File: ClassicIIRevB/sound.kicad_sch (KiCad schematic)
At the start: 56 parts, among them J1 SND OUT, J7 SND IN, Q2 MMBTA14, U1 MC34119, U11 LM3080, U2 78L08

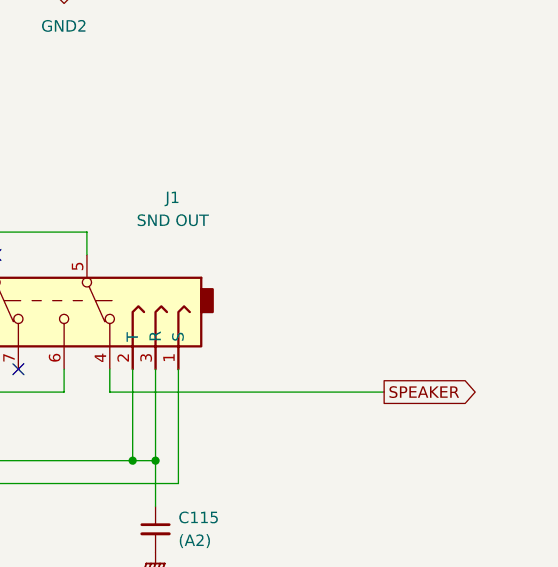
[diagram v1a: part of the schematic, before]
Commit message: improved footprints and silkscreens
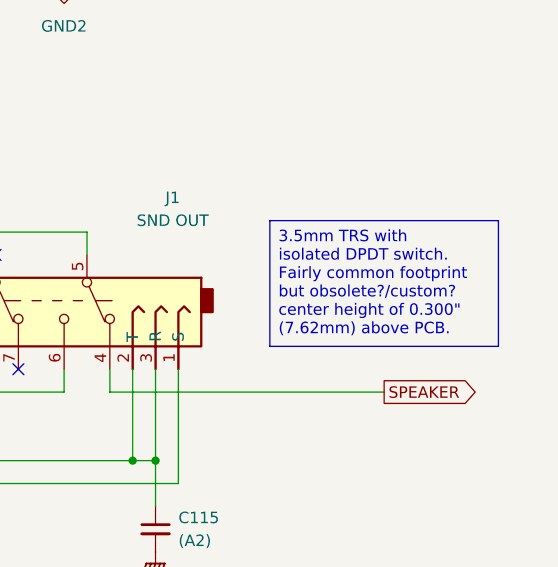
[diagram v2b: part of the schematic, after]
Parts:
- J1: footprint Connector_Mine:SJ3579AN -> Connector_Mine:Jack_3.5mm_SameSky_SJ3589ANG
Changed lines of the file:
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@@
 	(title_block
 		(title "Macintosh Classic II Revision B")
-		(date "2025-05-31")
+		(date "2025-06-04")
 		(company "Apple Computer")
 		(comment 1 "drawn by Bradley Bell")
@@
 		)
 	)
+	(text_box "3.5mm TRS with isolated DPDT switch.\nFairly common footprint but obsolete?/custom? center height of 0.300\" (7.62mm) above PCB."
+		(exclude_from_sim no)
+		(at 228.6 110.49 0)
+		(size 25.4 13.97)
+		(margins 0.9525 0.9525 0.9525 0.9525)
+		(stroke
+			(width 0)
+			(type solid)
+		)
+		(fill
+			(type none)
+		)
+		(effects
+			(font
+				(size 1.27 1.27)
+			)
+			(justify left top)
+		)
+	)
 	(junction
 		(at 165.1 137.16)
@@
 			)
 		)
-		(property "Footprint" "Connector_Mine:SJ3579AN"
+		(property "Footprint" "Connector_Mine:Jack_3.5mm_SameSky_SJ3589ANG"
 			(at 215.9 119.38 0)
 			(effects

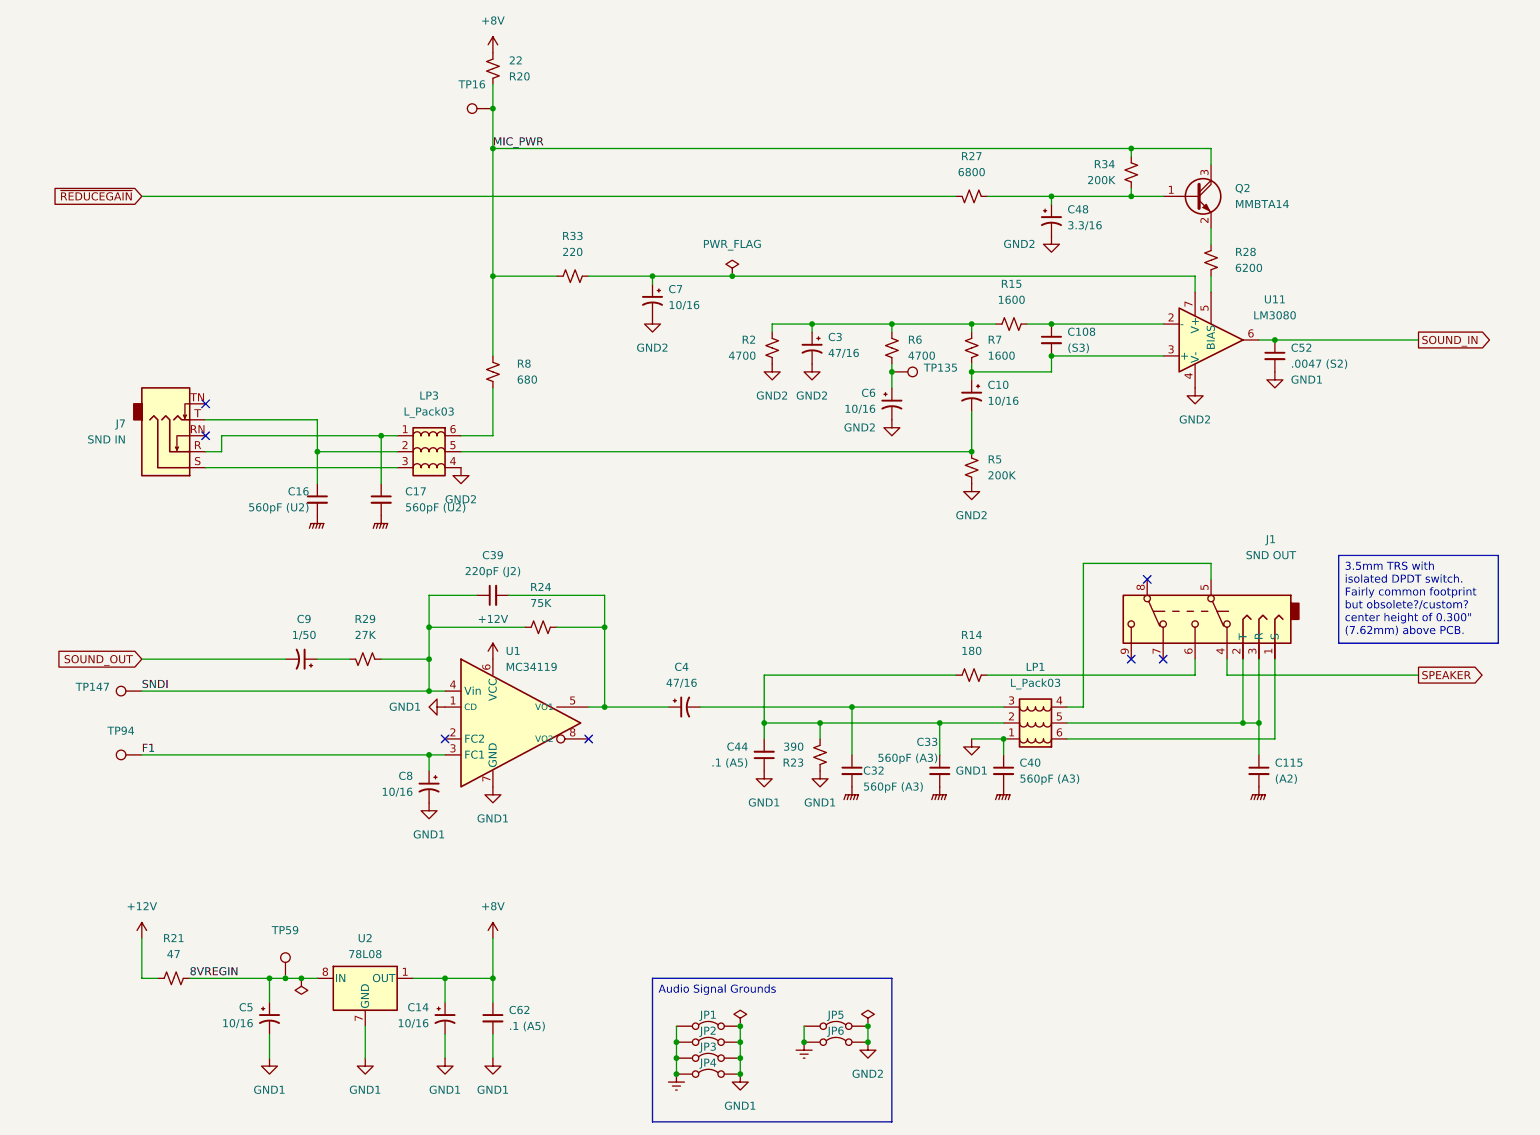
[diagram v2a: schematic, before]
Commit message: Switch to some "official" net names
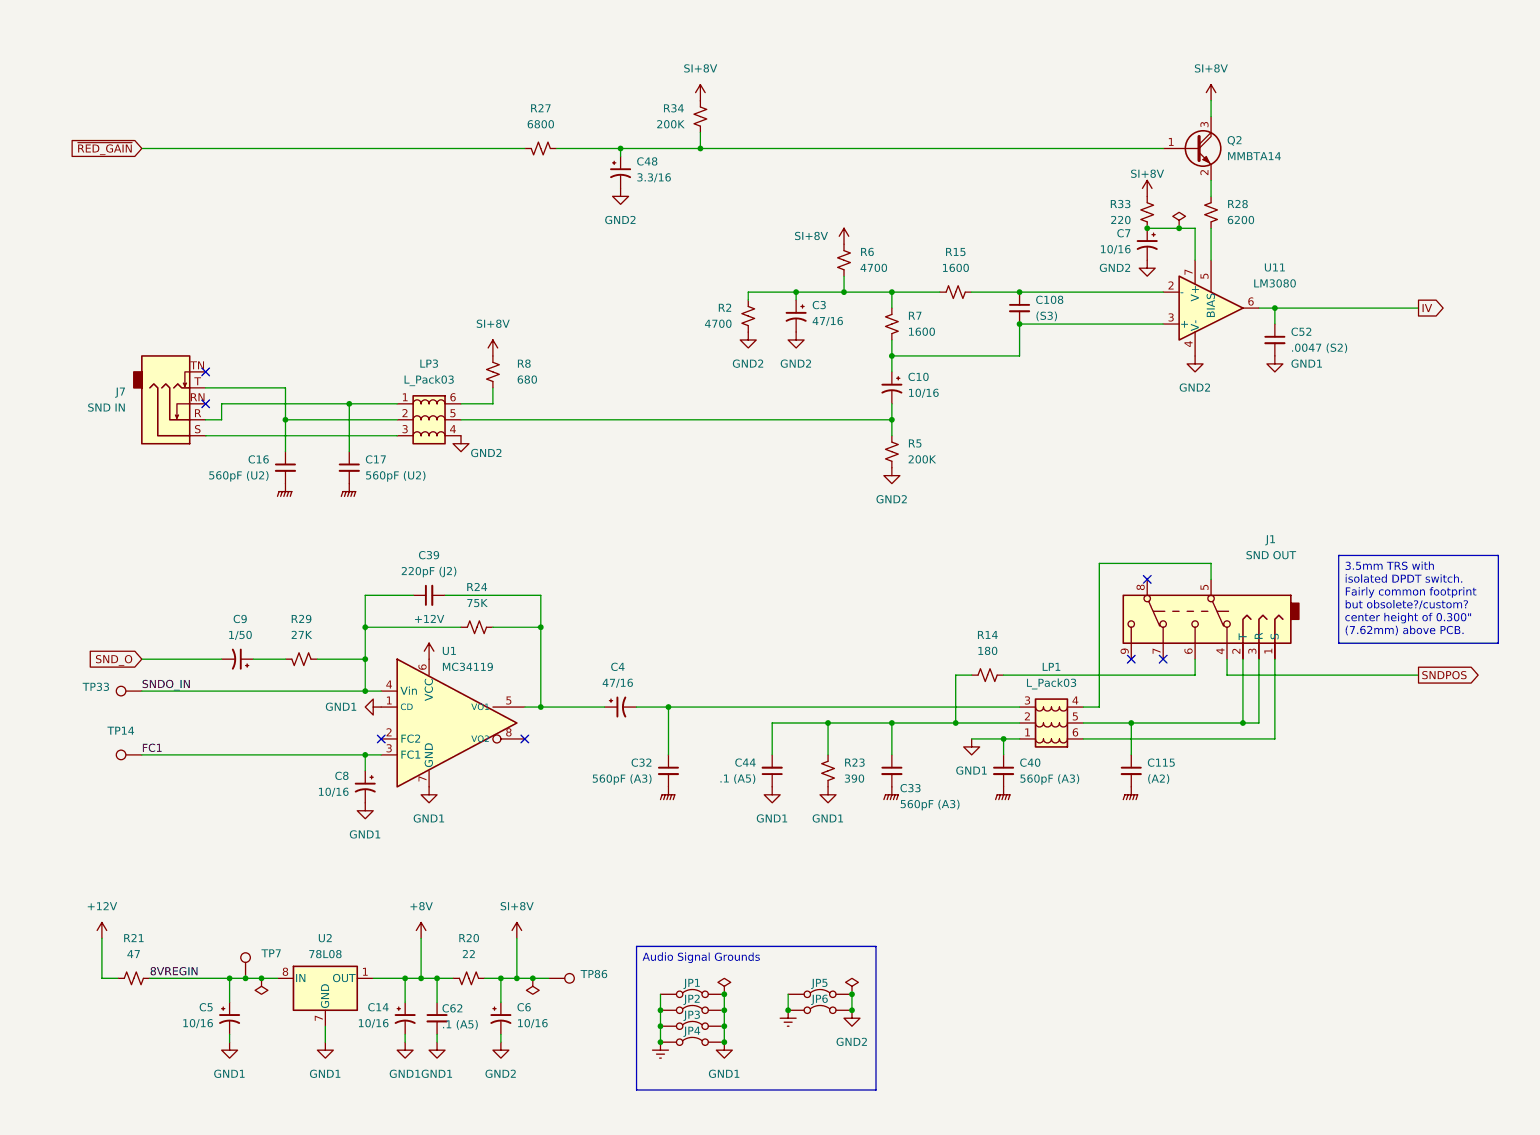
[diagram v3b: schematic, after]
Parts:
- removed TP135: ~, MyPackage:TestPoint_THTPad_D1.0mm_Drill0.5mm, symbol Connector:TestPoint
- renumbered TP94 to TP14, TP147 to TP33, TP59 to TP7, TP16 to TP86
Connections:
- net MIC_PWR is gone; now on net SI+8V: Q2.3 (C), R20.2, R33.2, R34.2, R8.2, TP86.1
- net SI+8V: now reaches C6.1, R6.2
- net F1 renamed FC1
- net SNDI renamed SNDO_IN
- net SOUND_IN renamed IV
- net SOUND_OUT renamed SND_O
- net SPEAKER renamed SNDPOS
- net ~{REDUCEGAIN} renamed ~{RED_GAIN}
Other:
- moved on the sheet: C10, C108, C115, C14, C16, C17, C3, C32, C33, C39, C4, C44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

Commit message: update exports
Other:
- title: Macintosh Classic II Revision B -> Macintosh Classic II (Later Revision)
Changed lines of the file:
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@@
 	(paper "USLetter")
 	(title_block
-		(title "Macintosh Classic II Revision B")
-		(date "2025-06-04")
+		(title "Macintosh Classic II (Later Revision)")
+		(date "2025-06-16")
 		(company "Apple Computer")
 		(comment 1 "drawn by Bradley Bell")

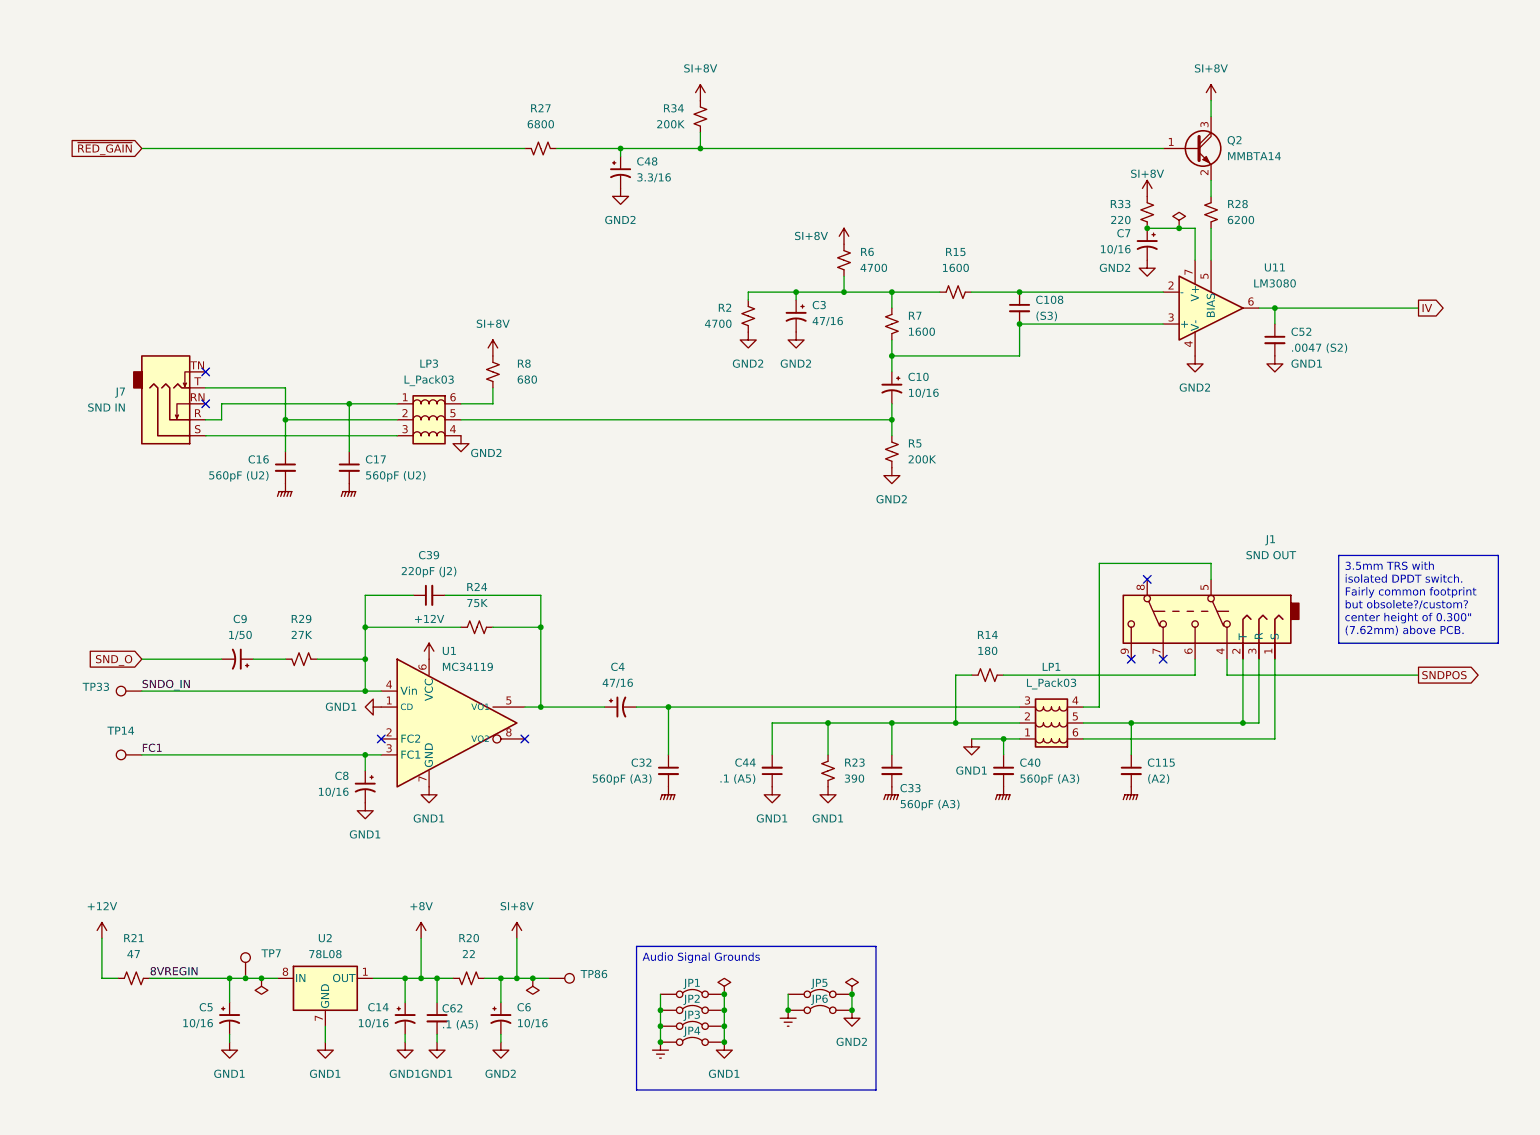
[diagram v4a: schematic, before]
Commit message: Corrections to SMDs, more improved footprints
The later revision board reproduction design is now complete.
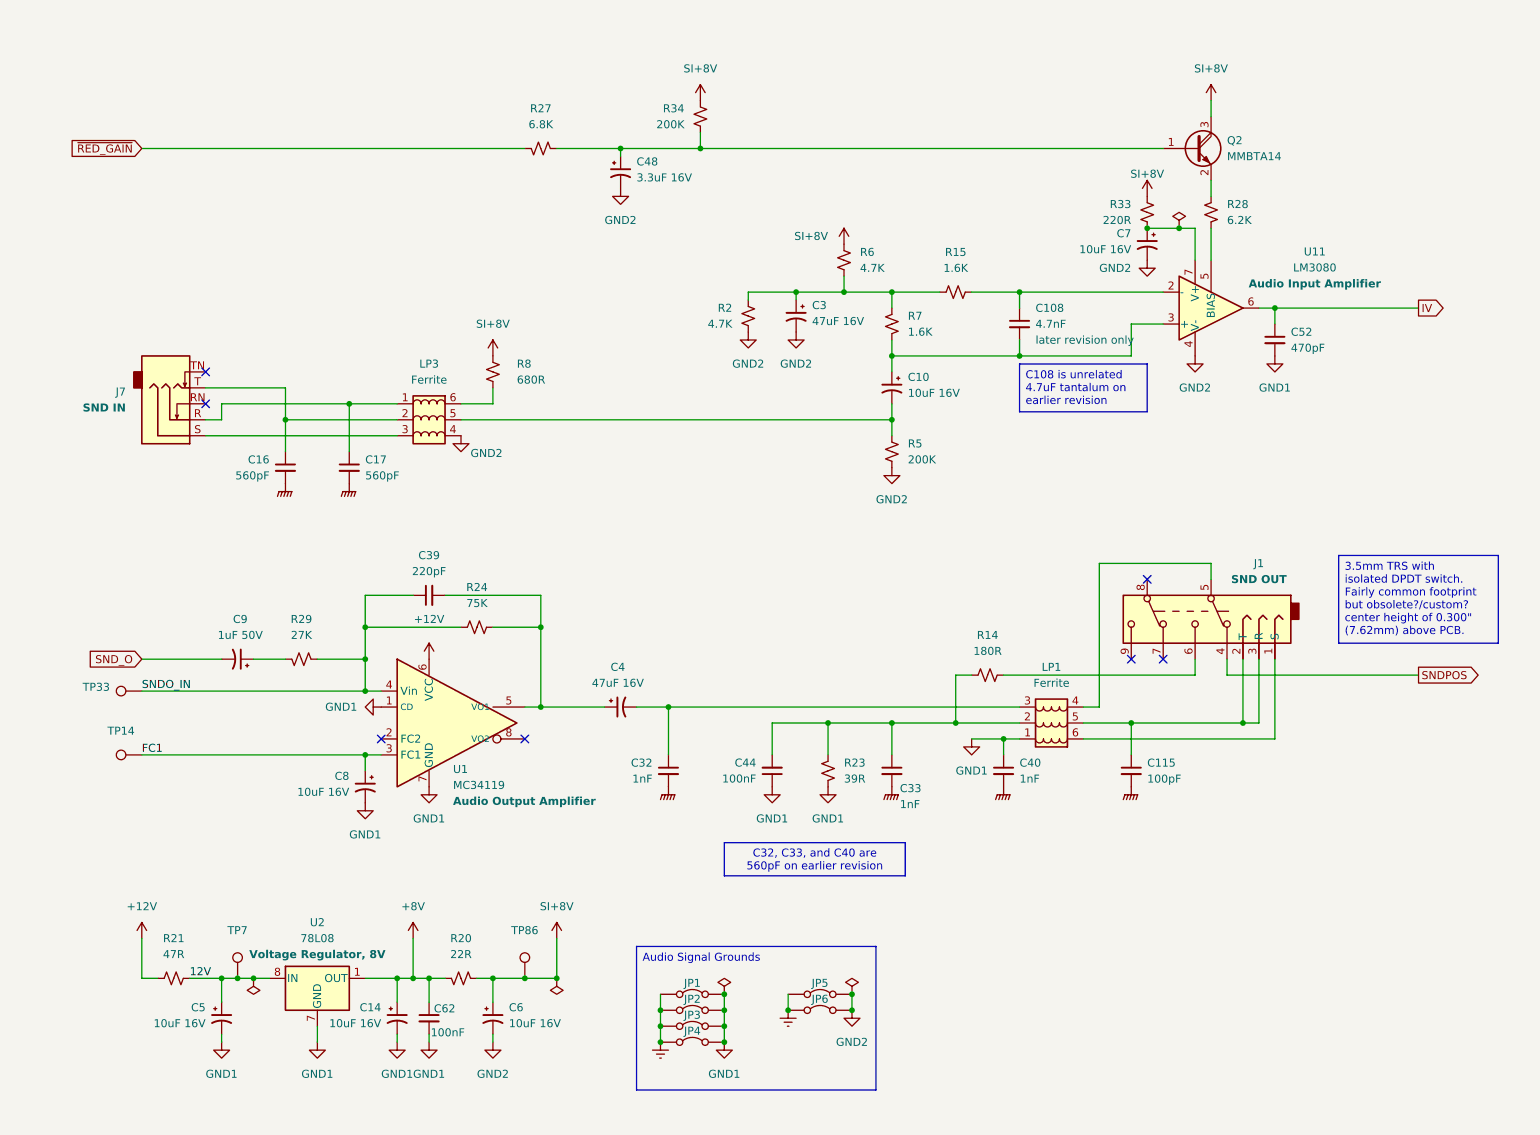
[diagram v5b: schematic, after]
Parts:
- C10, C14, C5, C6, C7, C8: value 10/16 -> 10uF 16V
- C108: value (S3) -> 4.7nF; Note (none) -> later revision only
- C115: value (A2) -> 100pF
- C16, C17: value 560pF (U2) -> 560pF
- C3, C4: value 47/16 -> 47uF 16V
- C32, C33, C40: value 560pF (A3) -> 1nF
- C39: value 220pF (J2) -> 220pF
- C44, C62: value .1 (A5) -> 100nF
- C48: value 3.3/16 -> 3.3uF 16V
- C52: value .0047 (S2) -> 470pF; Note (none) -> .0047 on bomarc, 470pF on official schematic
- C9: value 1/50 -> 1uF 50V
- J7: footprint Connector_Audio:Jack_3.5mm_CUI_SJ1-3535NG_Horizontal -> Connector_Mine:Jack_3.5mm_CUI_SJ1-3535NG_Horizontal
- JP1, JP2, JP3, JP4, JP5, JP6, TP14, TP33, TP7, TP86: now left out of the parts list
- LP1, LP3: value L_Pack03 -> Ferrite
- R14: value 180 -> 180R
- R15, R7: value 1600 -> 1.6K
- R2, R6: value 4700 -> 4.7K
- R20: value 22 -> 22R
- R21: value 47 -> 47R
- R23: value 390 -> 39R
- R27: value 6800 -> 6.8K
- R28: value 6200 -> 6.2K
- R33: value 220 -> 220R
- R8: value 680 -> 680R
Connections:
- net 8VREGIN renamed 12V
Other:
- moved on the sheet: C108, C14, C5, C6, C62, R20, R21, TP7, TP86, U2
